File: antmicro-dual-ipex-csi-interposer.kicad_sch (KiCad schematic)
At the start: 27 parts, among them J1 WE_68715014522, J2 MSAK24025P30, J3 MSAK24025P30

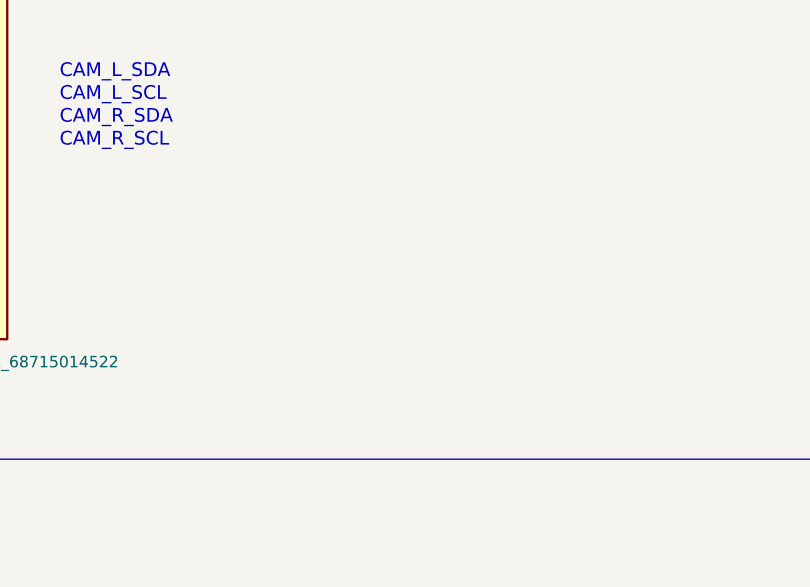
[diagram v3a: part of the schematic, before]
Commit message: Add decoupling, move all TP to the top
Cosmetic changes

Capital letter fix
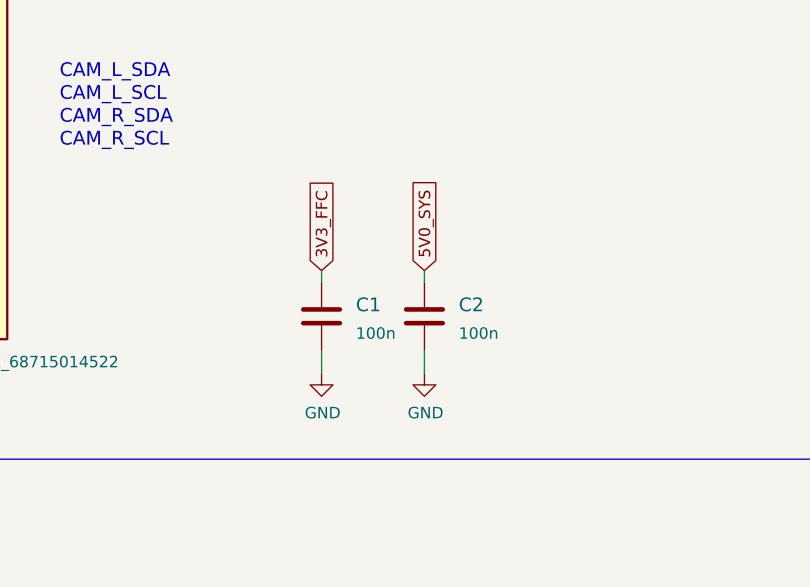
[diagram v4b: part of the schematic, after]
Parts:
- added C1, C2: C_100n_0402, antmicro-footprints:0402-cap, symbol antmicroCapacitors0402:C_100n_0402
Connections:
- net 3V3_FFC: now also C1.1
- net 5V0_SYS: now also C2.1
- net GND: now also C1.2, C2.2
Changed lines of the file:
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@@
+    (stroke (width 0) (type default) (color 0 0 0 0))
+  )
+  (wire (pts (xy 339.09 184.15) (xy 339.09 185.42))
     (stroke (width 0) (type default) (color 0 0 0 0))
   )
@@
     (stroke (width 0) (type default) (color 0 0 0 0))
   )
+  (wire (pts (xy 350.52 193.04) (xy 350.52 195.58))
+    (stroke (width 0) (type default) (color 0 0 0 0))
+  )
   (wire (pts (xy 284.48 187.96) (xy 290.83 187.96))
     (stroke (width 0) (type default) (color 0 0 0 0))
@@
     (stroke (width 0) (type default) (color 0 0 0 0))
   )
+  (wire (pts (xy 350.52 184.15) (xy 350.52 185.42))
+    (stroke (width 0) (type default) (color 0 0 0 0))
+  )
   (wire (pts (xy 69.215 79.375) (xy 62.23 79.375))
     (stroke (width 0) (type default) (color 0 0 0 0))
@@
   )
   (wire (pts (xy 274.955 167.64) (xy 297.815 167.64))
+    (stroke (width 0) (type default) (color 0 0 0 0))
+  )
+  (wire (pts (xy 339.09 193.04) (xy 339.09 195.58))
     (stroke (width 0) (type default) (color 0 0 0 0))
   )
@@
     )
   )
+  (global_label "3V3_FFC" (shape input) (at 339.09 184.15 90) (fields_autoplaced)
+    (effects (font (size 1.27 1.27)) (justify left))
+    (property "Intersheet References" "${INTERSHEET_REFS}" (id 0) (at 521.97 -100.33 0)
+      (effects (font (size 1.27 1.27)) hide)
+    )
+  )
   (global_label "CAM1_CSI_D2_N" (shape input) (at 46.355 81.915 180) (fields_autoplaced)
     (effects (font (size 1.27 1.27)) (justify right))
@@
     (property "Intersheet References" "${INTERSHEET_REFS}" (id 0) (at 129.6046 99.6156 0)
       (effects (font (size 1.27 1.27)) (justify right) hide)
+    )
+  )
+  (global_label "5V0_SYS" (shape input) (at 350.52 184.15 90) (fields_autoplaced)
+    (effects (font (size 1.27 1.27)) (justify left))
+    (property "Intersheet References" "${INTERSHEET_REFS}" (id 0) (at 538.48 -100.33 0)
+      (effects (font (size 1.27 1.27)) hide)
     )
   )
@@
     (pin "1")
   )
+  (symbol (lib_id "antmicroCapacitors0402:C_100n_0402") (at 339.09 189.23 0) (unit 1)
+    (in_bom yes) (on_board yes) (fields_autoplaced)
+    (property "Reference" "C1" (id 0) (at 342.9 187.96 0)
+      (effects (font (size 1.524 1.524)) (justify left))
+    )
+    (property "Value" "C_100n_0402" (id 1) (at 339.09 193.04 0)
+      (effects (font (size 1.524 1.524)) hide)
+    )
+    (property "Footprint" "antmicro-footprints:0402-cap" (id 2) (at 344.17 184.15 0)
+      (effects (font (size 1.524 1.524)) (justify left) hide)
+    )
+    (property "Datasheet" "" (id 3) (at 339.09 189.23 0)
+      (effects (font (size 1.27 1.27)) hide)
+    )
+    (property "Manufacturer" "Murata" (id 4) (at 344.17 179.07 0)
+      (effects (font (size 1.524 1.524)) (justify left) hide)
+    )
+    (property "MPN" "GRM155R61H104KE14D" (id 5) (at 344.17 181.61 0)
+      (effects (font (size 1.524 1.524)) (justify left) hide)
+    )
+    (property "Val" "100n" (id 6) (at 342.9 191.1349 0)
+      (effects (font (size 1.27 1.27)) (justify left))
+    )
+    (pin "1")
+    (pin "2")
+  )
   (symbol (lib_id "antmicroResistors0402:R_0R_0402") (at 261.62 153.67 0) (unit 1)
     (in_bom yes) (on_board yes)
@@
     (pin "9")
   )
+  (symbol (lib_id "antmicroCapacitors0402:C_100n_0402") (at 350.52 189.23 0) (unit 1)
+    (in_bom yes) (on_board yes) (fields_autoplaced)
+    (property "Reference" "C2" (id 0) (at 354.33 187.96 0)
+      (effects (font (size 1.524 1.524)) (justify left))
+    )
+    (property "Value" "C_100n_0402" (id 1) (at 350.52 193.04 0)
+      (effects (font (size 1.524 1.524)) hide)
+    )
+    (property "Footprint" "antmicro-footprints:0402-cap" (id 2) (at 355.6 184.15 0)
+      (effects (font (size 1.524 1.524)) (justify left) hide)
+    )
+    (property "Datasheet" "" (id 3) (at 350.52 189.23 0)
+      (effects (font (size 1.27 1.27)) hide)
+    )
+    (property "Manufacturer" "Murata" (id 4) (at 355.6 179.07 0)
+      (effects (font (size 1.524 1.524)) (justify left) hide)
+    )
+    (property "MPN" "GRM155R61H104KE14D" (id 5) (at 355.6 181.61 0)
+      (effects (font (size 1.524 1.524)) (justify left) hide)
+    )
+    (property "Val" "100n" (id 6) (at 354.33 191.1349 0)
+      (effects (font (size 1.27 1.27)) (justify left))
+    )
+    (pin "1")
+    (pin "2")
+  )
   (symbol (lib_id "antmicroResistors0402:R_0R_0402") (at 261.62 162.56 0) (unit 1)
     (in_bom yes) (on_board yes)
@@
     (pin "2")
   )
+  (symbol (lib_id "antmicro-dual-ipex-csi-interposer-rescue:GND-framos-csi-interposer") (at 350.52 195.58 0) (unit 1)
+    (in_bom yes) (on_board yes)
+    (property "Reference" "#PWR0103" (id 0) (at 350.52 201.93 0)
+      (effects (font (size 1.27 1.27)) hide)
+    )
+    (property "Value" "GND" (id 1) (at 350.647 199.9742 0))
+    (property "Footprint" "" (id 2) (at 350.52 195.58 0)
+      (effects (font (size 1.27 1.27)) hide)
+    )
+    (property "Datasheet" "" (id 3) (at 350.52 195.58 0)
+      (effects (font (size 1.27 1.27)) hide)
+    )
+    (pin "1")
+  )
   (symbol (lib_id "antmicroResistors0402:R_0R_0402") (at 261.62 146.05 0) (unit 1)
     (in_bom yes) (on_board yes)
@@
     (pin "1")
     (pin "2")
+  )
+  (symbol (lib_id "antmicro-dual-ipex-csi-interposer-rescue:GND-framos-csi-interposer") (at 339.09 195.58 0) (unit 1)
+    (in_bom yes) (on_board yes)
+    (property "Reference" "#PWR0104" (id 0) (at 339.09 201.93 0)
+      (effects (font (size 1.27 1.27)) hide)
+    )
+    (property "Value" "GND" (id 1) (at 339.217 199.9742 0))
+    (property "Footprint" "" (id 2) (at 339.09 195.58 0)
+      (effects (font (size 1.27 1.27)) hide)
+    )
+    (property "Datasheet" "" (id 3) (at 339.09 195.58 0)
+      (effects (font (size 1.27 1.27)) hide)
+    )
+    (pin "1")
   )
   (sheet_instances
@@
       (reference "#PWR0102") (unit 1) (value "GND") (footprint "")
     )
+    (path "/a46ad373-10a1-4d1f-8ac5-39fbb5e8b997"
+      (reference "#PWR0103") (unit 1) (value "GND") (footprint "")
+    )
+    (path "/e89a4f31-f7d8-45c6-84f3-7af7149bc281"
+      (reference "#PWR0104") (unit 1) (value "GND") (footprint "")
+    )
+    (path "/713bb508-48a9-4007-a154-31041fc2d5c1"
+      (reference "C1") (unit 1) (value "C_100n_0402") (footprint "antmicro-footprints:0402-cap")
+    )
+    (path "/87577648-9f5c-41b6-8058-9cb0e120403a"
+      (reference "C2") (unit 1) (value "C_100n_0402") (footprint "antmicro-footprints:0402-cap")
+    )
     (path "/00000000-0000-0000-0000-000061f21fbc"

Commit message: Generate loclib. Cleanup
Add boards image. Add image link to README
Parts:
- C1, C2: footprint antmicro-footprints:0402-cap -> antmicro-dual-ipex-csi-interposer-footprints:0402-cap; symbol antmicroCapacitors0402:C_100n_0402 -> antmicro-dual-ipex-csi-interposer:C_100n_0402
- J1: footprint antmicro-footprints:WE_68715014522 -> antmicro-dual-ipex-csi-interposer-footprints:WE_68715014522; symbol antmicroFCCConnectors:WE_68715014522 -> antmicro-dual-ipex-csi-interposer:WE_68715014522
- J2, J3: footprint antmicro-footprints:MSAK24025P30 -> antmicro-dual-ipex-csi-interposer-footprints:MSAK24025P30; symbol antmicroFCCConnectors:MSAK24025P30 -> antmicro-dual-ipex-csi-interposer:MSAK24025P30
- MP1, MP2, MP3, MP4: footprint antmicro-footprints:mounting-hole-2.2mm -> antmicro-dual-ipex-csi-interposer-footprints:mounting-hole-2.2mm; symbol antmicroMechanicalParts:PCB_Mount_Hole_2.2_4.5 -> antmicro-dual-ipex-csi-interposer:PCB_Mount_Hole_2.2_4.5
- N1: footprint antmicro-footprints:oshw-logo -> antmicro-dual-ipex-csi-interposer-footprints:oshw-logo; symbol antmicroMechanicalParts:oshw_logo -> antmicro-dual-ipex-csi-interposer:oshw_logo
- N2: footprint antmicro-footprints:antmicro-logo_scaled_12mm -> antmicro-dual-ipex-csi-interposer-footprints:antmicro-logo_scaled_12mm; symbol antmicroMechanicalParts:antmicro_logo -> antmicro-dual-ipex-csi-interposer:antmicro_logo
- R1, R2, R3, R4, R5, R6, R7, R8: footprint antmicro-footprints:0402-res -> antmicro-dual-ipex-csi-interposer-footprints:0402-res; symbol antmicroResistors0402:R_0R_0402 -> antmicro-dual-ipex-csi-interposer:R_0R_0402
- TP1, TP10, TP2, TP3, TP4, TP5, TP6, TP7, TP8, TP9: footprint antmicro-footprints:Testpoint_smd_1mm -> antmicro-dual-ipex-csi-interposer-footprints:Testpoint_smd_1mm; symbol antmicroTestPoints:TP_SMD1MM -> antmicro-dual-ipex-csi-interposer:TP_SMD1MM
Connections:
- no-connect marks 18 -> 15
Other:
- moved on the sheet: MP1, MP2, MP3, MP4, R1, R2, R3, R4, R6, R8, TP4, TP5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
